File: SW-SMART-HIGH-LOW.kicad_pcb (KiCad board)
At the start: 2 copper layers, 72 x 69 mm, 36 parts, among them IC1 MCP1416, J1 SWLINK, J2 USART1, SW1 BTS50010-1TAD, SW2 VNB35N07xx-E, U1 STM32G0B1KBTx, U4 MCP2562-E-SN

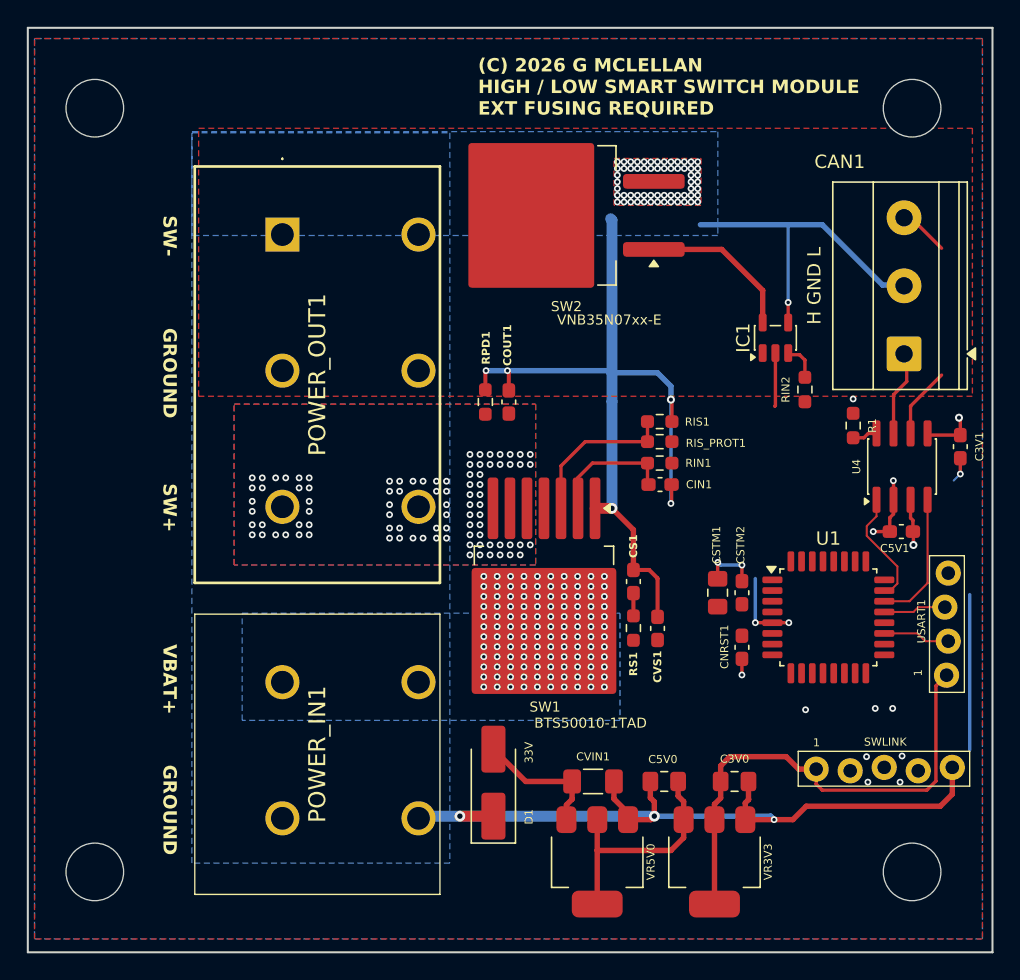
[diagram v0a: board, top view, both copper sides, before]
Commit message: routing power and data nets
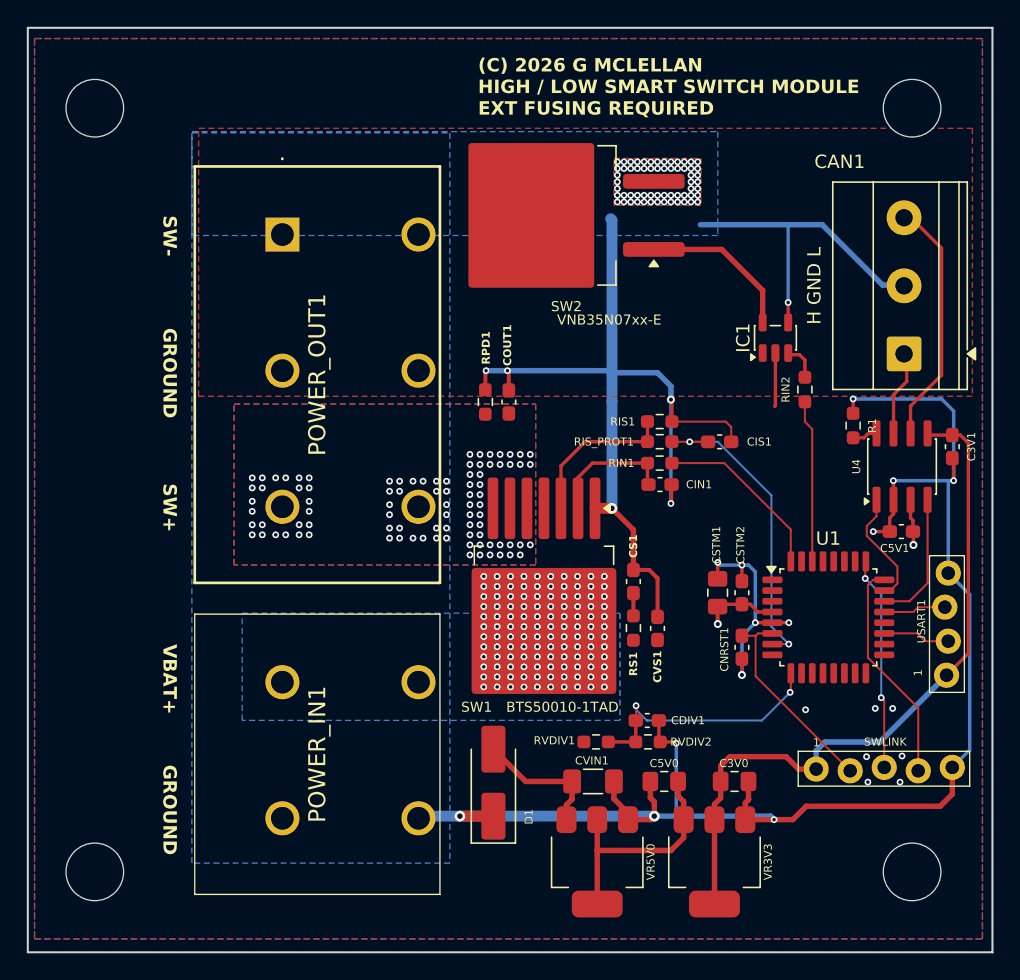
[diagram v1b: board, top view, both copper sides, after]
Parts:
- added CDIV1: 100n, Capacitor_SMD:C_0603_1608Metric_Pad1.08x0.95mm_HandSolder, F.Cu at (127.2, 117.7)
- added CIS1: 100n, Capacitor_SMD:C_0603_1608Metric_Pad1.08x0.95mm_HandSolder, F.Cu at (132.6, 96.9)
- added RVDIV1: 10K, Resistor_SMD:R_0603_1608Metric_Pad0.98x0.95mm_HandSolder, F.Cu at (123.4, 119.3)
- added RVDIV2: 4K7, Resistor_SMD:R_0603_1608Metric_Pad0.98x0.95mm_HandSolder, F.Cu at (127.3, 119.3)
- moved C3V1 0.60 mm to (150.0, 97.3)
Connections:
- RIN1 pad 1: unconnected-(RIN1-Pad1) -> /SW1IN
- RIN2 pad 1: unconnected-(RIN2-Pad1) -> /SW2IN
- RIS_PROT1 pad 1: unconnected-(RIS_PROT1-Pad1) -> /SW1IS
- U1 pad 30: unconnected-(U1-PB6-Pad30) -> /SW2IN
- U1 pad 32: unconnected-(U1-PB8-Pad32) -> /SW1IN
- U1 pad 7: unconnected-(U1-PA0-Pad7) -> /SW1IS
- U1 pad 9: unconnected-(U1-PA2-Pad9) -> /VS
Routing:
- net GND: track 175.6 -> 225.1 mm, vias 79 -> 80
- net /SW1IS: track 0.00 -> 23.3 mm, vias 0 -> 2
- net /VS: track 0.00 -> 19.2 mm, vias 0 -> 2
- net +3.3V: track 40.9 -> 58.8 mm
- net /SWDIO: track 0.00 -> 16.8 mm
- net /SWCLK: track 0.00 -> 16.0 mm, vias 0 -> 2
- net /NRST: track 0.00 -> 15.3 mm
- net /SW1IN: track 0.00 -> 13.3 mm
- net /SW2IN: track 0.00 -> 12.1 mm
- net /CAN_L: track 9.06 -> 18.5 mm

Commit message: I think the layout is complete
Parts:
- renumbered R1 to RSTBY1
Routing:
- net +5V: track 21.0 -> 61.0 mm, vias 1 -> 2
- net +3.3V: track 58.8 -> 70.0 mm
- net GND: track 225.1 -> 228.9 mm, vias 80 -> 77

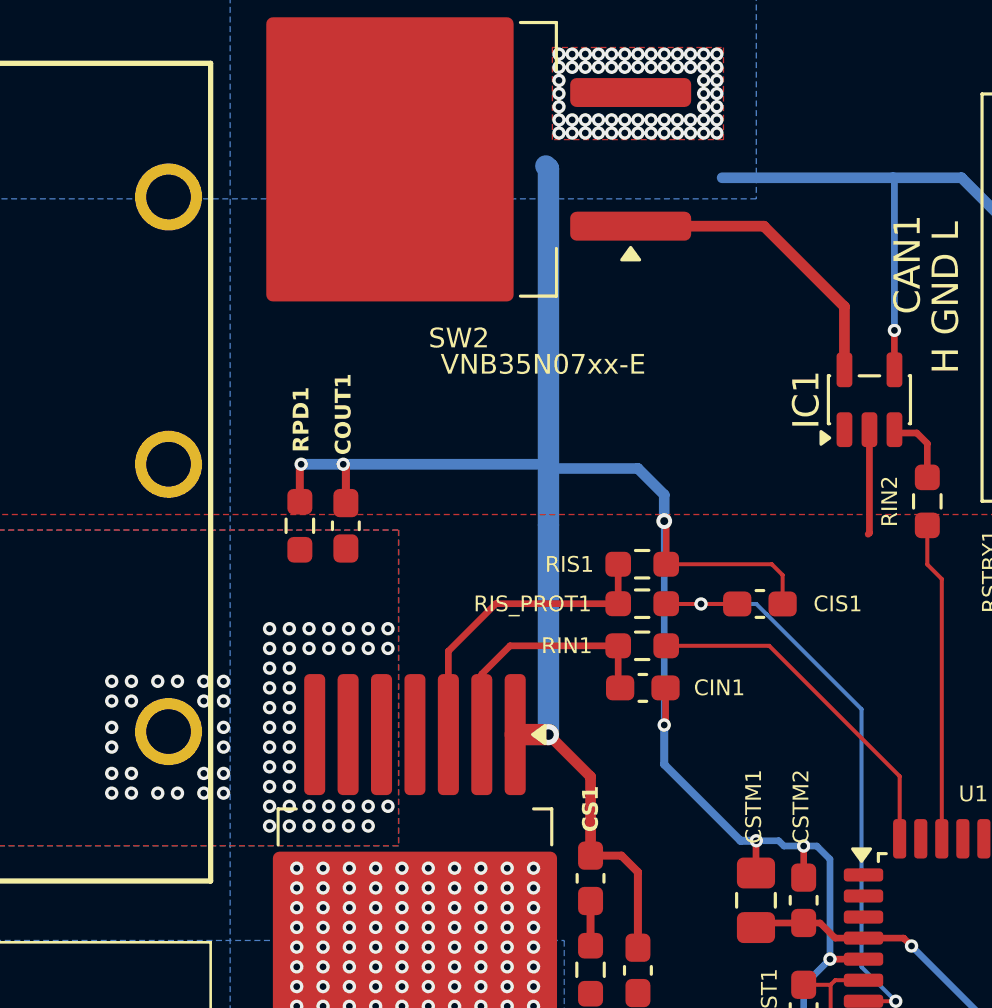
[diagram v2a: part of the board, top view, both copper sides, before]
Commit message: clean up ground tracks
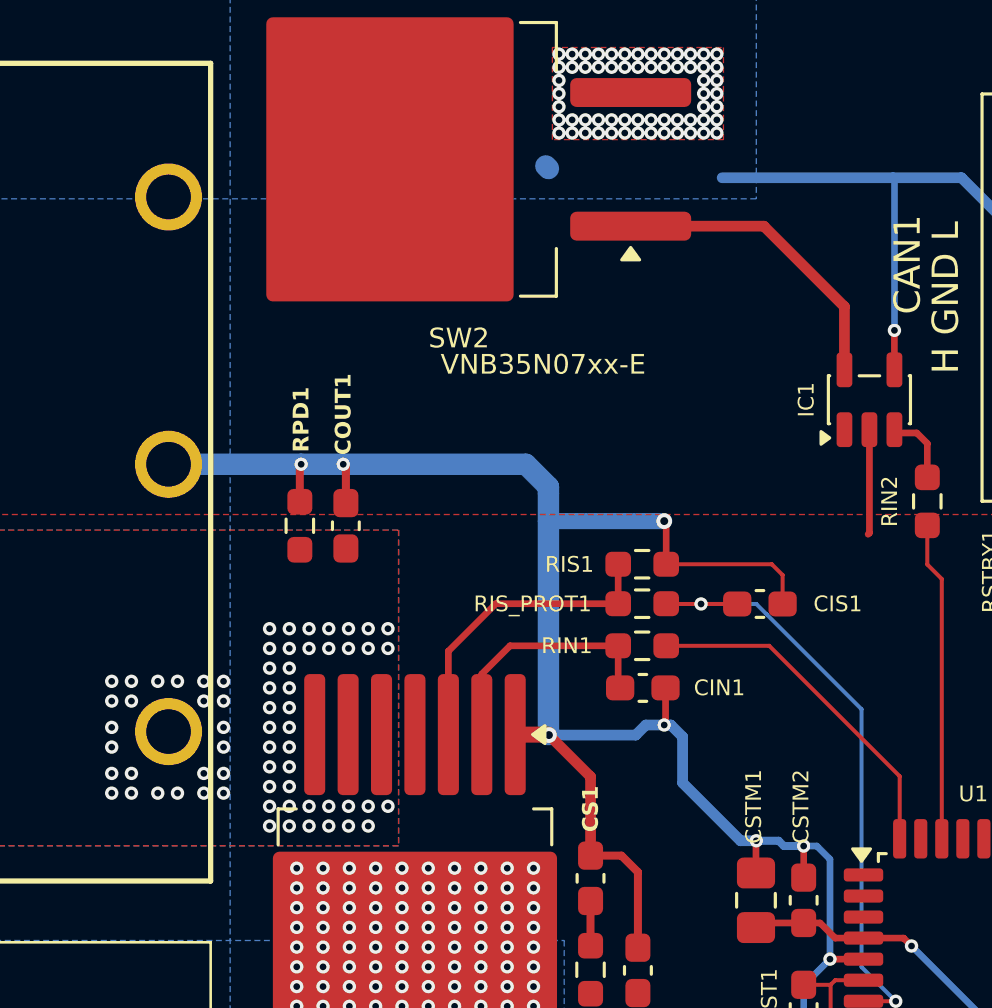
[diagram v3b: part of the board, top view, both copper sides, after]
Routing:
- net GND: track 228.9 -> 217.6 mm
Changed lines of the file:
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@@
 			(effects
 				(font
-					(size 1 1)
-					(thickness 0.15)
+					(size 0.6 0.6)
+					(thickness 0.1)
 				)
 			)
@@
 	)
 	(segment
+		(start 129 93.75)
+		(end 129.075 93.825)
+		(width 0.254)
+		(layer "F.Cu")
+		(net 1)
+	)
+	(segment
 		(start 128 107.09)
 		(end 128 109.965)
@@
 	)
 	(segment
+		(start 124.6175 101.8825)
+		(end 124.6 101.865)
+		(width 0.406)
+		(layer "F.Cu")
+		(net 1)
+	)
+	(segment
 		(start 125.8 125.1)
 		(end 127.5 125.1)
@@
 	)
 	(segment
-		(start 124.6 101.865)
-		(end 123.335 101.865)
-		(width 0.8128)
-		(layer "F.Cu")
-		(net 1)
-	)
-	(segment
 		(start 128.2 119.3)
 		(end 129.3 119.3)
@@
 	)
 	(segment
-		(start 129 93.75)
-		(end 129.075 93.825)
-		(width 0.254)
-		(layer "F.Cu")
-		(net 1)
-	)
-	(segment
 		(start 116.9 91.69)
 		(end 116.8 91.59)
@@
 	)
 	(segment
+		(start 129.075 93.825)
+		(end 129.075 95.39)
+		(width 0.254)
+		(layer "F.Cu")
+		(net 1)
+	)
+	(segment
 		(start 126.2 106.465)
 		(end 126.2 103.465)
@@
 	)
 	(segment
-		(start 129.075 93.825)
-		(end 129.075 95.39)
-		(width 0.254)
-		(layer "F.Cu")
-		(net 1)
-	)
-	(segment
 		(start 116.9 93.065)
 		(end 116.9 91.69)
@@
 	)
 	(segment
+		(start 123.335 101.865)
+		(end 124.6 101.865)
+		(width 0.61)
+		(layer "F.Cu")
+		(net 1)
+	)
+	(segment
 		(start 134.55 125.1)
 		(end 136.7 125.1)
@@
 	(segment
 		(start 126.2 103.465)
-		(end 124.6 101.865)
+		(end 124.6175 101.8825)
 		(width 0.406)
 		(layer "F.Cu")
@@
 	)
 	(via
-		(at 124.6 101.865)
-		(size 0.8)
-		(drill 0.4)
-		(layers "F.Cu" "B.Cu")
-		(tenting none)
-		(net 1)
-	)
-	(via
 		(at 127.5 78.5)
 		(size 0.508)
@@
 	)
 	(via
+		(at 124.6175 101.8825)
+		(size 0.6)
+		(drill 0.3)
+		(layers "F.Cu" "B.Cu")
+		(net 1)
+	)
+	(via
 		(at 125 78)
 		(size 0.508)
@@
 	)
 	(segment
-		(start 129 93.75)
-		(end 129 92.75)
+		(start 131.9 105.9)
+		(end 129.7 103.7)
 		(width 0.406)
 		(layer "B.Cu")
@@
 	)
 	(segment
-		(start 129 103)
-		(end 129 101.5)
-		(width 0.305)
-		(layer "B.Cu")
-		(net 1)
-	)
-	(segment
 		(start 133.35 105.9)
 		(end 132.5 105.9)
-		(width 0.254)
-		(layer "B.Cu")
-		(net 1)
-	)
-	(segment
-		(start 124.6 93.89)
-		(end 124.6 101.865)
-		(width 0.8128)
+		(width 0.305)
 		(layer "B.Cu")
 		(net 1)
@@
 	)
 	(segment
-		(start 124.6 91.75)
-		(end 124.6 80.35)
+		(start 124.6 92.7)
+		(end 124.6 92.45)
 		(width 0.8128)
 		(layer "B.Cu")
@@
 	)
 	(segment
+		(start 129.25 101.5)
+		(end 129 101.5)
+		(width 0.406)
+		(layer "B.Cu")
+		(net 1)
+	)
+	(segment
 		(start 133.55 106.1)
 		(end 133.35 105.9)
-		(width 0.254)
+		(width 0.305)
 		(layer "B.Cu")
 		(net 1)
@@
 	)
 	(segment
-		(start 124.44 91.59)
-		(end 124.6 91.75)
-		(width 0.61)
+		(start 115.2 91.59)
+		(end 110.16 91.59)
+		(width 0.8128)
 		(layer "B.Cu")
 		(net 1)
 	)
 	(segment
-		(start 115.2 91.59)
-		(end 124.44 91.59)
+		(start 127.9175 101.8825)
+		(end 124.6175 101.8825)
+		(width 0.406)
+		(layer "B.Cu")
+		(net 1)
+	)
+	(segment
+		(start 129 101.5)
+		(end 128.3 101.5)
 		(width 0.406)
 		(layer "B.Cu")
@@
 	)
 	(segment
-		(start 134.3 106.1)
-		(end 133.55 106.1)
-		(width 0.254)
+		(start 124.6 92.45)
+		(end 123.74 91.59)
+		(width 0.8128)
 		(layer "B.Cu")
 		(net 1)
 	)
 	(segment
-		(start 149.7 106.7)
-		(end 149.7 100.2)
-		(width 0.254)
+		(start 132.5 105.9)
+		(end 131.9 105.9)
+		(width 0.406)
 		(layer "B.Cu")
 		(net 1)
 	)
 	(segment
-		(start 132.5 105.9)
-		(end 131.9 105.9)
+		(start 134.3 106.1)
+		(end 133.55 106.1)
 		(width 0.305)
 		(layer "B.Cu")
@@
 	)
 	(segment
-		(start 149.2 93.7)
-		(end 142.6 93.7)
-		(width 0.254)
+		(start 129.7 101.95)
+		(end 129.25 101.5)
+		(width 0.406)
 		(layer "B.Cu")
 		(net 1)
 	)
 	(segment
-		(start 129 101.5)
-		(end 129 93.75)
+		(start 149.7 106.7)
+		(end 149.7 100.2)
 		(width 0.254)
 		(layer "B.Cu")
@@
 	)
 	(segment
-		(start 129 92.75)
-		(end 128 91.75)
-		(width 0.406)
+		(start 149.2 93.7)
+		(end 142.6 93.7)
+		(width 0.254)
 		(layer "B.Cu")
 		(net 1)
@@
 	)
 	(segment
+		(start 124.6 92.7)
+		(end 124.6 93.75)
+		(width 0.8128)
+		(layer "B.Cu")
+		(net 1)
+	)
+	(segment
 		(start 137.7 80.7)
 		(end 131.2 80.7)
@@
 	)
 	(segment
-		(start 128 91.75)
-		(end 124.6 91.75)
-		(width 0.406)
+		(start 123.74 91.59)
+		(end 115.2 91.59)
+		(width 0.8128)
 		(layer "B.Cu")
 		(net 1)
@@
 	)
 	(segment
-		(start 131.9 105.9)
-		(end 129 103)
-		(width 0.305)
+		(start 129.4 119.4)
+		(end 129.4 124.84)
+		(width 0.254)
 		(layer "B.Cu")
 		(net 1)
 	)
 	(segment
-		(start 129.4 119.4)
-		(end 129.4 124.84)
-		(width 0.254)
+		(start 129.7 103.7)
+		(end 129.7 101.95)
+		(width 0.406)
 		(layer "B.Cu")
 		(net 1)
@@
 	)
 	(segment
+		(start 124.6 93.75)
+		(end 124.6 101.865)
+		(width 0.8128)
+		(layer "B.Cu")
+		(net 1)
+	)
+	(segment
 		(start 144.8 85.2)
 		(end 140.3 80.7)
@@
 	)
 	(segment
+		(start 128.3 101.5)
+		(end 127.9175 101.8825)
+		(width 0.406)
+		(layer "B.Cu")
+		(net 1)
+	)
+	(segment
 		(start 150.1 99.8)
 		(end 150.1 94.6)
@@
 	)
 	(segment
-		(start 124.6 93.89)
-		(end 124.6 91.75)
-		(width 0.8128)
+		(start 129 93.75)
+		(end 124.6 93.75)
+		(width 0.61)
 		(layer "B.Cu")
 		(net 1)
